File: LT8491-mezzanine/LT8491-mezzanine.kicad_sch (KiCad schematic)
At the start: 122 parts, among them J1 Conn_01x01, J10 Conn_01x01, J11 Conn_01x01, J12 Conn_01x01, J13 Conn_01x01, J14 Conn_01x01, J15 Conn_01x01, J16 Conn_01x01, J17 Conn_01x01, J18 Conn_01x01, J19 Conn_01x01, J2 Conn_01x01, J20 Conn_01x01, J21 Conn_01x01, J22 Conn_01x01, J23 Conn_01x01, J24 Conn_01x01, J25 Conn_01x01, J3 Conn_01x01, J4 Conn_01x01, J5 Conn_01x01, J6 Conn_01x01, J7 Conn_01x01, J8 Conn_01x01, J9 Conn_01x01, Q1 SIS128LDN-T1-GE3, Q2 SIS128LDN-T1-GE3, Q3 SIS128LDN-T1-GE3, Q4 SIS128LDN-T1-GE3, Q5 BSS138DWQ-7, Q6 MBT2222ADW1T1, U4 LT8491IUKJPBF

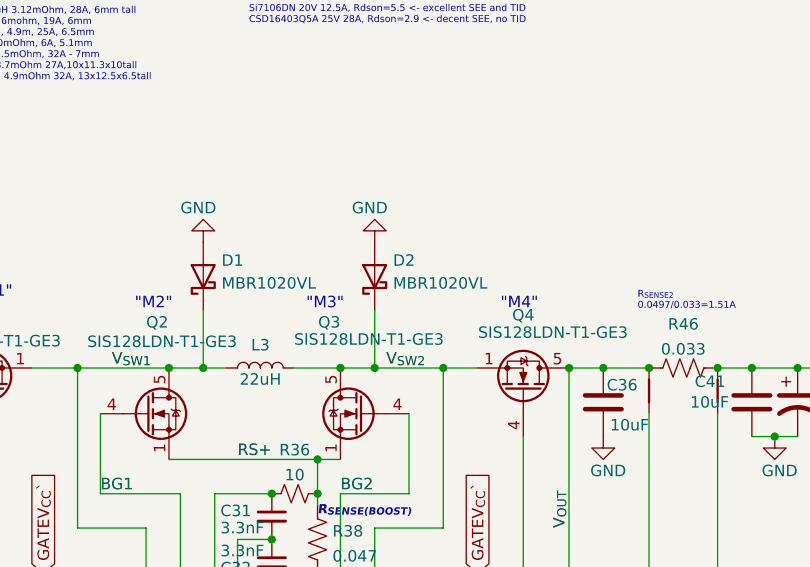
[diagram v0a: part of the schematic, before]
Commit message: changed the schottkey diode to the right one and changed footprint of really small resistors
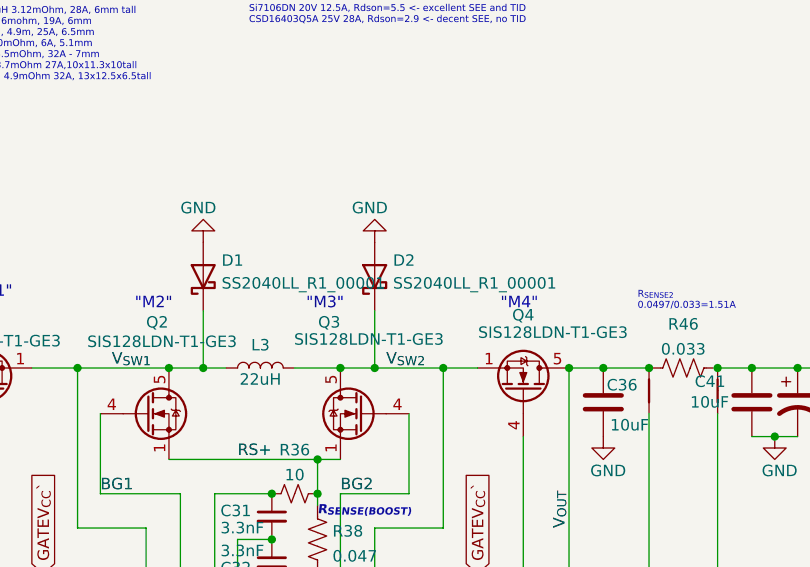
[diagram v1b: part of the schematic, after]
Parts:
- D1, D2: value MBR1020VL -> SS2040LL_R1_00001
- Q5, Q6, R3, R4, R53, R54, R55, R56, R57, R58: now left out of the parts list
- R5, R6: footprint Resistor_SMD:R_0402_1005Metric -> Resistor_SMD:R_0603_1608Metric; now left out of the parts list

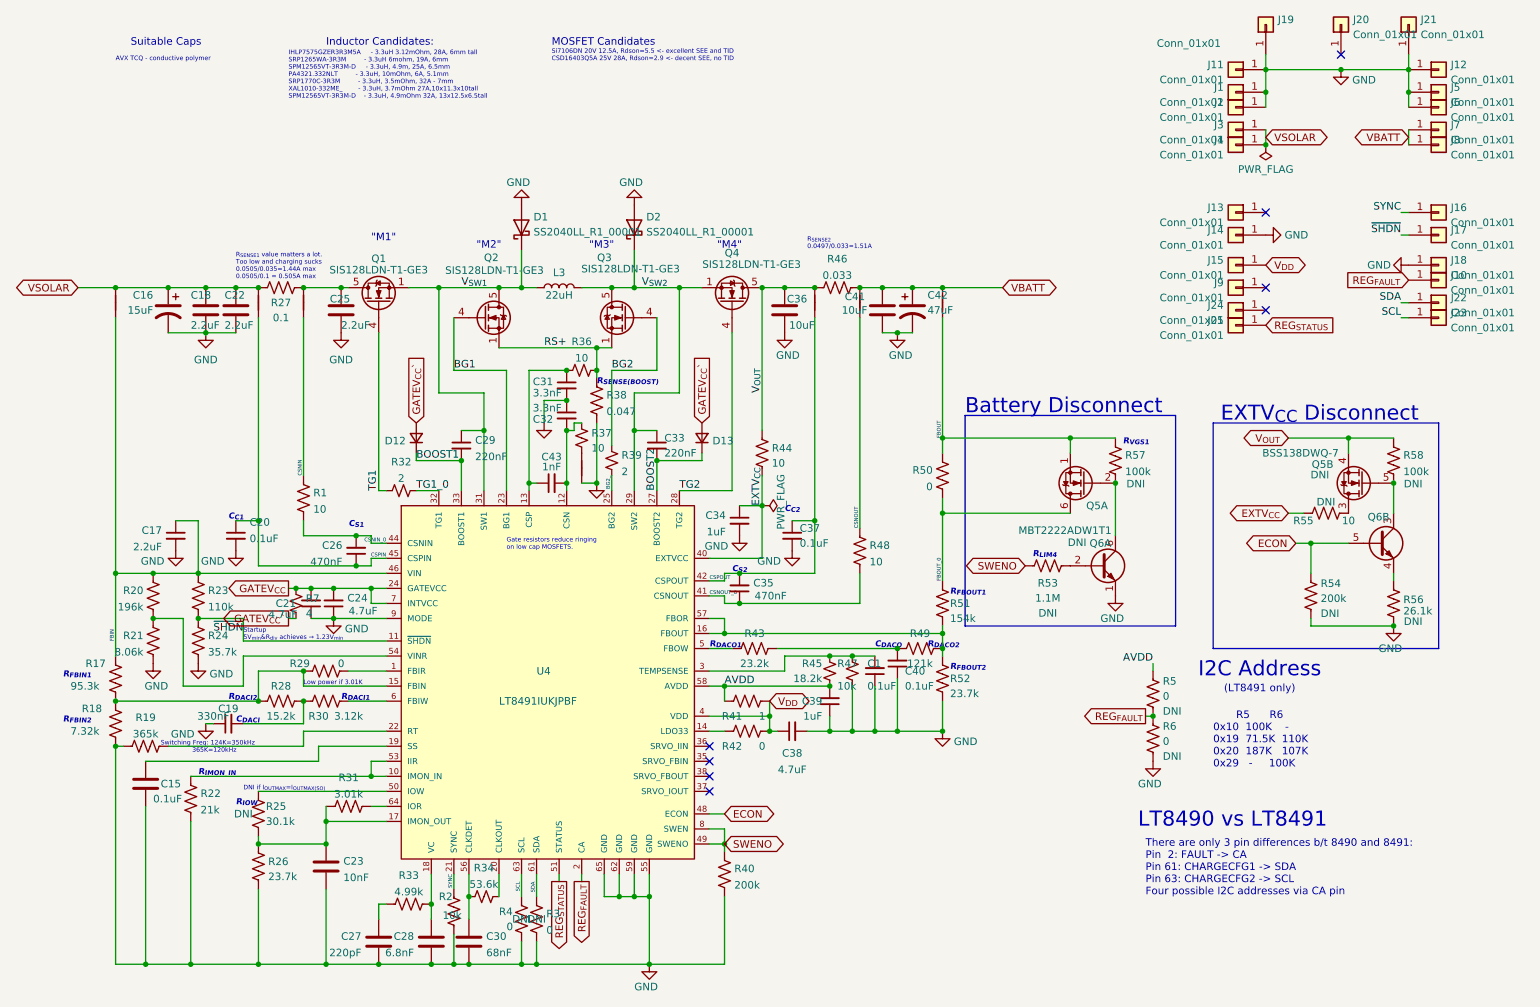
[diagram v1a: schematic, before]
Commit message: updated LT8491-mezzanine (MPPT) to Kicad 9, flex panel schematic PDF name, jobsets back to original ordering (issue was elsewhere)
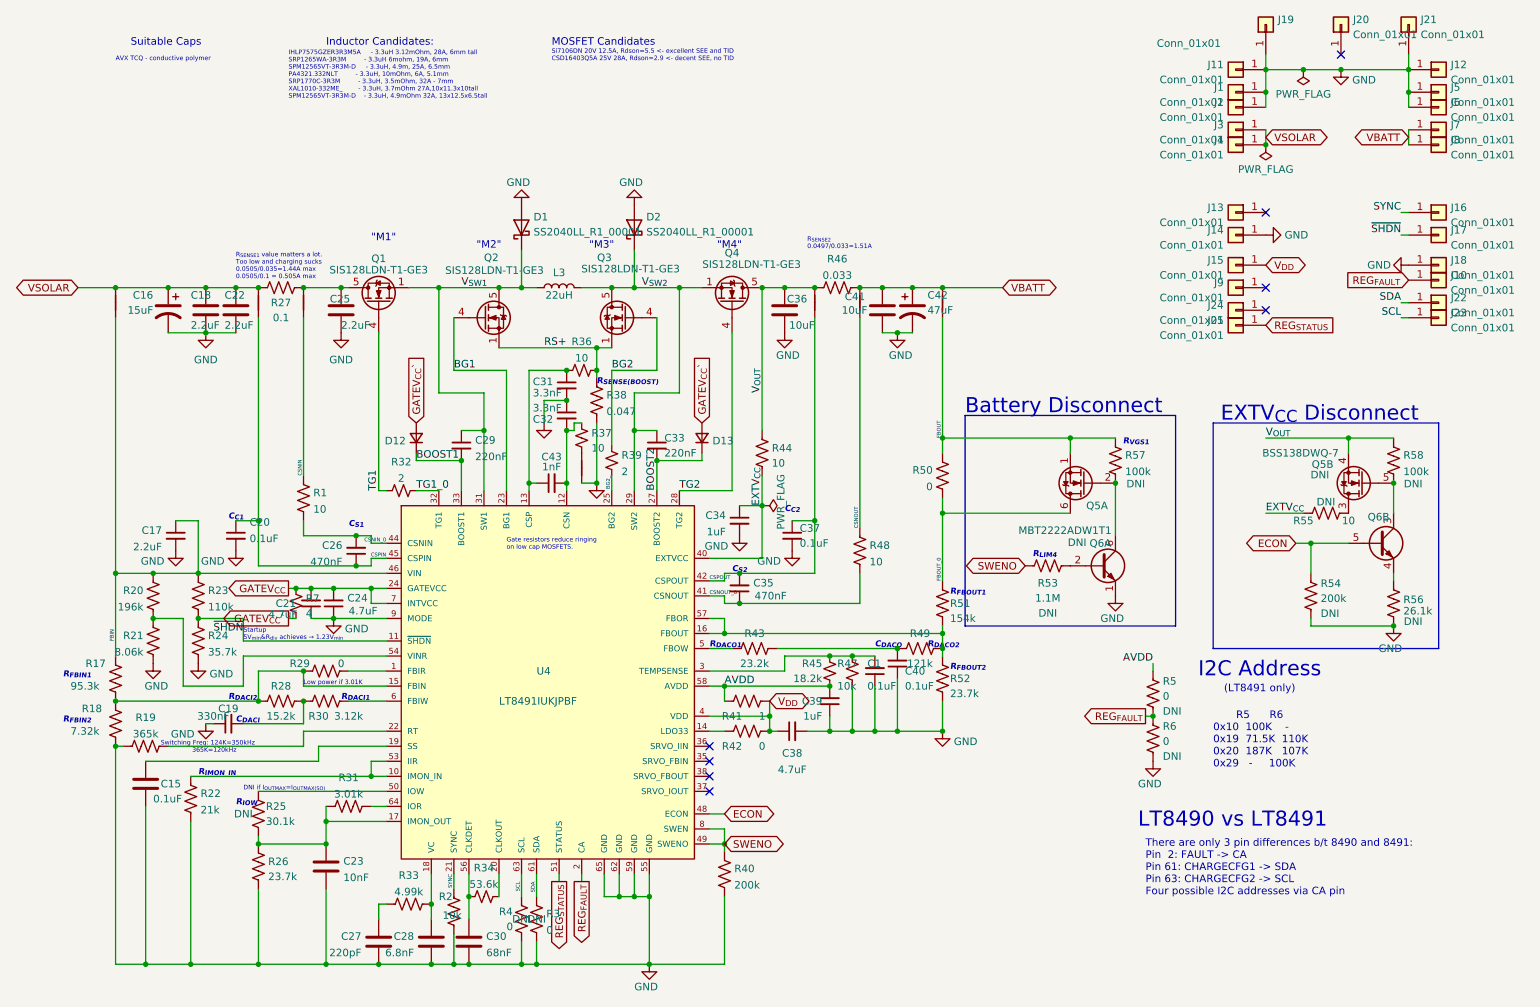
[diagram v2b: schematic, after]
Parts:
- Q5: Height 1.1 -> (none); Mouser Part Number 621-BSS138DWQ-7 -> (none); Mouser Price/Stock https://www.mouser.co.uk/ProductDetail/Diodes-Incorporated/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 -> (none)
- Q6: now in the parts list
